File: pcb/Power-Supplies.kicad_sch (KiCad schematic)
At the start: 19 parts, among them U4 TLV62568DRL, U6 TLV75533PDRV, U7 TLV62568DRL

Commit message: Rev A Updates
Support LD2410S and LD2420 Radars in same connector as C4001. Now using 3.3V instead of 5V.
Removed Power control for Radars.
Added DS18S20 to measure CO sensor temperature directly.
Reworked SHT4X layout to reduce thermal transfer.
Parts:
- renumbered C14 to C10, C15 to C11, C16 to C12, C18 to C14, C19 to C15, C20 to C16, C21 to C17, C22 to C18, C23 to C19, C13 to C9, R3 to R1, R4 to R2, R6 to R4, R7 to R5, U4 to U2, U6 to U4, U7 to U5
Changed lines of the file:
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@@
 	(title_block
 		(title "ESPHome Parking Assistant")
-		(date "2025-04-18")
-		(rev "A")
+		(date "2025-09-23")
+		(rev "B")
 		(company "Mike Lawrence")
 	)
@@
 		(on_board yes)
 		(dnp no)
-		(property "Reference" "C16"
+		(property "Reference" "C12"
 			(at 152.4 128.524 0)
 			(effects
@@
 			(project "ESPHome-Indoor-Multi-Sensor"
 				(path "/e74956a0-c576-42e7-be96-7ce5c3135988/3a60bf96-310e-40eb-add5-f40abb45b52a"
-					(reference "C16")
+					(reference "C12")
 					(unit 1)
 				)
@@
 		(on_board yes)
 		(dnp no)
-		(property "Reference" "C14"
+		(property "Reference" "C10"
 			(at 129.54 128.524 0)
 			(effects
@@
 			(project "ESPHome-Indoor-Multi-Sensor"
 				(path "/e74956a0-c576-42e7-be96-7ce5c3135988/3a60bf96-310e-40eb-add5-f40abb45b52a"
-					(reference "C14")
+					(reference "C10")
 					(unit 1)
 				)
@@
 		(on_board yes)
 		(dnp no)
-		(property "Reference" "C20"
+		(property "Reference" "C16"
 			(at 95.25 65.024 0)
 			(effects
@@
 			(project "ESPHome-Indoor-Multi-Sensor"
 				(path "/e74956a0-c576-42e7-be96-7ce5c3135988/3a60bf96-310e-40eb-add5-f40abb45b52a"
-					(reference "C20")
+					(reference "C16")
 					(unit 1)
 				)
@@
 		(on_board yes)
 		(dnp no)
-		(property "Reference" "C21"
+		(property "Reference" "C17"
 			(at 154.94 65.024 0)
 			(effects
@@
 			(project "ESPHome-Indoor-Multi-Sensor"
 				(path "/e74956a0-c576-42e7-be96-7ce5c3135988/3a60bf96-310e-40eb-add5-f40abb45b52a"
-					(reference "C21")
+					(reference "C17")
 					(unit 1)
 				)
@@
 		(on_board yes)
 		(dnp no)
-		(property "Reference" "R7"
+		(property "Reference" "R5"
 			(at 144.018 69.85 0)
 			(effects
@@
 			(project "ESPHome-Indoor-Multi-Sensor"
 				(path "/e74956a0-c576-42e7-be96-7ce5c3135988/3a60bf96-310e-40eb-add5-f40abb45b52a"
-					(reference "R7")
+					(reference "R5")
 					(unit 1)
 				)
@@
 		(on_board yes)
 		(dnp no)
-		(property "Reference" "C13"
+		(property "Reference" "C9"
 			(at 69.85 128.524 0)
 			(effects
@@
 			(project "ESPHome-Indoor-Multi-Sensor"
 				(path "/e74956a0-c576-42e7-be96-7ce5c3135988/3a60bf96-310e-40eb-add5-f40abb45b52a"
-					(reference "C13")
+					(reference "C9")
 					(unit 1)
 				)
@@
 		(on_board yes)
 		(dnp no)
-		(property "Reference" "C22"
+		(property "Reference" "C18"
 			(at 166.37 65.024 0)
 			(effects
@@
 			(project "ESPHome-Indoor-Multi-Sensor"
 				(path "/e74956a0-c576-42e7-be96-7ce5c3135988/3a60bf96-310e-40eb-add5-f40abb45b52a"
-					(reference "C22")
+					(reference "C18")
 					(unit 1)
 				)
@@
 		(on_board yes)
 		(dnp no)
-		(property "Reference" "U6"
+		(property "Reference" "U4"
 			(at 177.8 112.014 0)
 			(effects
@@
 			(project ""
 				(path "/e74956a0-c576-42e7-be96-7ce5c3135988/3a60bf96-310e-40eb-add5-f40abb45b52a"
-					(reference "U6")
+					(reference "U4")
 					(unit 1)
 				)
@@
 		(on_board yes)
 		(dnp no)
-		(property "Reference" "R3"
+		(property "Reference" "R1"
 			(at 118.618 123.19 0)
 			(effects
@@
 			(project "ESPHome-Indoor-Multi-Sensor"
 				(path "/e74956a0-c576-42e7-be96-7ce5c3135988/3a60bf96-310e-40eb-add5-f40abb45b52a"
-					(reference "R3")
+					(reference "R1")
 					(unit 1)
 				)
@@
 		(on_board yes)
 		(dnp no)
-		(property "Reference" "C19"
+		(property "Reference" "C15"
 			(at 203.2 128.524 0)
 			(effects
@@
 			(project "ESPHome-Indoor-Multi-Sensor"
 				(path "/e74956a0-c576-42e7-be96-7ce5c3135988/3a60bf96-310e-40eb-add5-f40abb45b52a"
-					(reference "C19")
+					(reference "C15")
 					(unit 1)
 				)
@@
 		(on_board yes)
 		(dnp no)
-		(property "Reference" "R6"
+		(property "Reference" "R4"
 			(at 144.018 59.69 0)
 			(effects
@@
 			(project "ESPHome-Indoor-Multi-Sensor"
 				(path "/e74956a0-c576-42e7-be96-7ce5c3135988/3a60bf96-310e-40eb-add5-f40abb45b52a"
-					(reference "R6")
+					(reference "R4")
 					(unit 1)
 				)
@@
 		(on_board yes)
 		(dnp no)
-		(property "Reference" "U7"
+		(property "Reference" "U5"
 			(at 114.3 48.006 0)
 			(effects
@@
 			(project "ESPHome-Indoor-Multi-Sensor"
 				(path "/e74956a0-c576-42e7-be96-7ce5c3135988/3a60bf96-310e-40eb-add5-f40abb45b52a"
-					(reference "U7")
+					(reference "U5")
 					(unit 1)
 				)
@@
 		(on_board yes)
 		(dnp no)
-		(property "Reference" "C15"
+		(property "Reference" "C11"
 			(at 140.97 128.524 0)
 			(effects
@@
 			(project "ESPHome-Indoor-Multi-Sensor"
 				(path "/e74956a0-c576-42e7-be96-7ce5c3135988/3a60bf96-310e-40eb-add5-f40abb45b52a"
-					(reference "C15")
+					(reference "C11")
 					(unit 1)
 				)
@@
 		(on_board yes)
 		(dnp no)
-		(property "Reference" "C23"
+		(property "Reference" "C19"
 			(at 177.8 65.024 0)
 			(effects
@@
 			(project "ESPHome-Indoor-Multi-Sensor"
 				(path "/e74956a0-c576-42e7-be96-7ce5c3135988/3a60bf96-310e-40eb-add5-f40abb45b52a"
-					(reference "C23")
+					(reference "C19")
 					(unit 1)
 				)
@@
 		(on_board yes)
 		(dnp no)
-		(property "Reference" "U4"
+		(property "Reference" "U2"
 			(at 88.9 111.506 0)
 			(effects
@@
 			(project "ESPHome-Indoor-Multi-Sensor"
 				(path "/e74956a0-c576-42e7-be96-7ce5c3135988/3a60bf96-310e-40eb-add5-f40abb45b52a"
-					(reference "U4")
+					(reference "U2")
 					(unit 1)
 				)
@@
 		(on_board yes)
 		(dnp no)
-		(property "Reference" "R4"
+		(property "Reference" "R2"
 			(at 118.618 133.35 0)
 			(effects
@@
 			(project "ESPHome-Indoor-Multi-Sensor"
 				(path "/e74956a0-c576-42e7-be96-7ce5c3135988/3a60bf96-310e-40eb-add5-f40abb45b52a"
-					(reference "R4")
+					(reference "R2")
 					(unit 1)
 				)
@@
 		(on_board yes)
 		(dnp no)
-		(property "Reference" "C18"
+		(property "Reference" "C14"
 			(at 191.77 128.524 0)
 			(effects
@@
 			(project "ESPHome-Indoor-Multi-Sensor"
 				(path "/e74956a0-c576-42e7-be96-7ce5c3135988/3a60bf96-310e-40eb-add5-f40abb45b52a"
-					(reference "C18")
+					(reference "C14")
 					(unit 1)
 				)

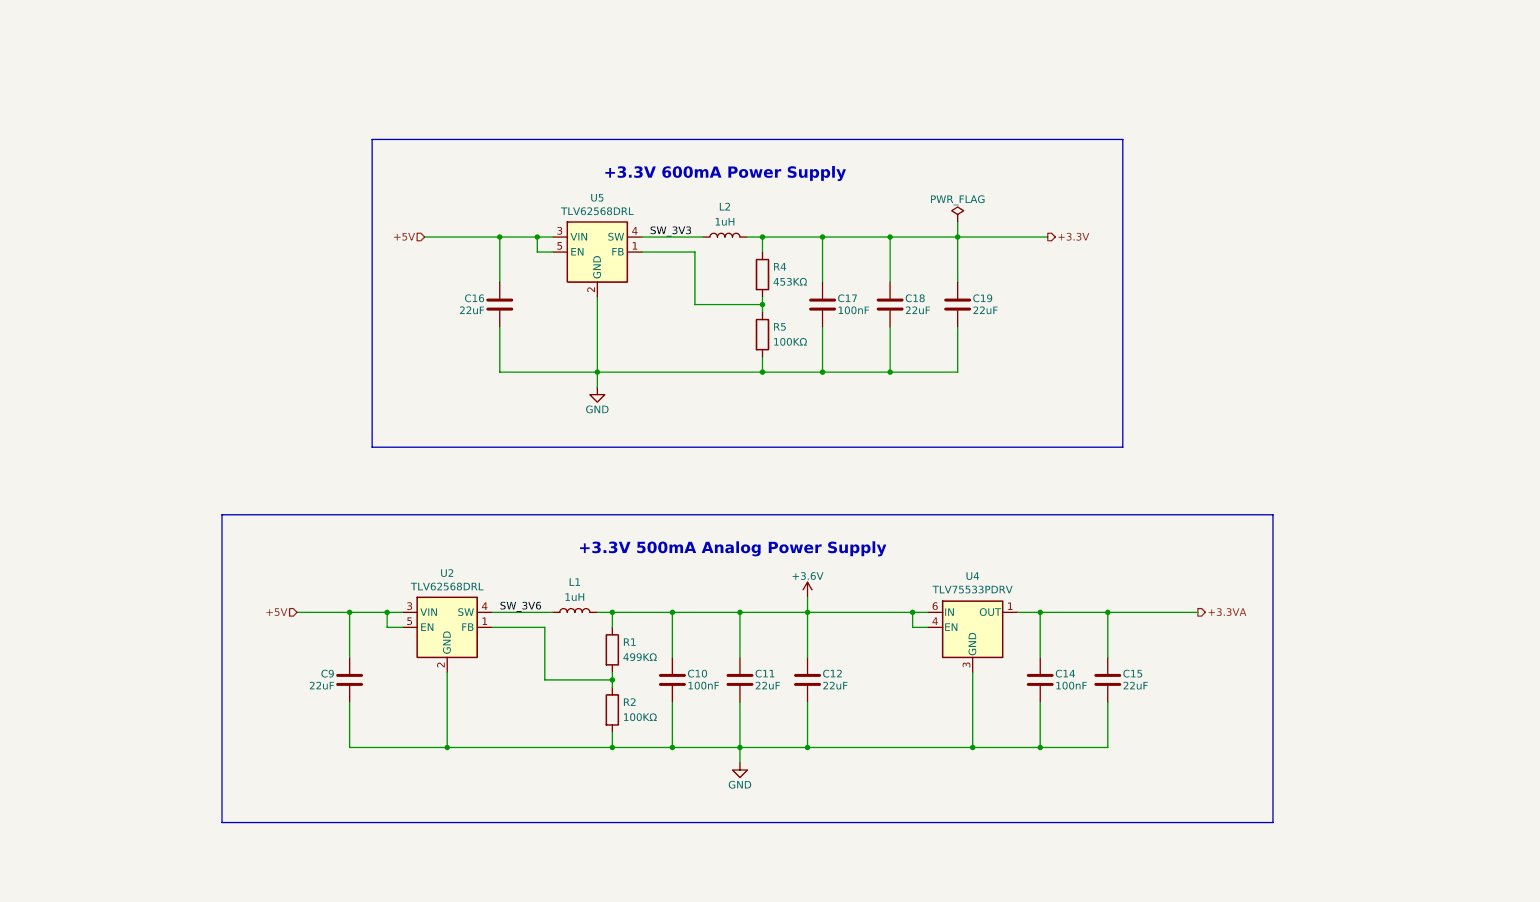
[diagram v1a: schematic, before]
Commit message: Add new ina228 to other power supplies
Not finished
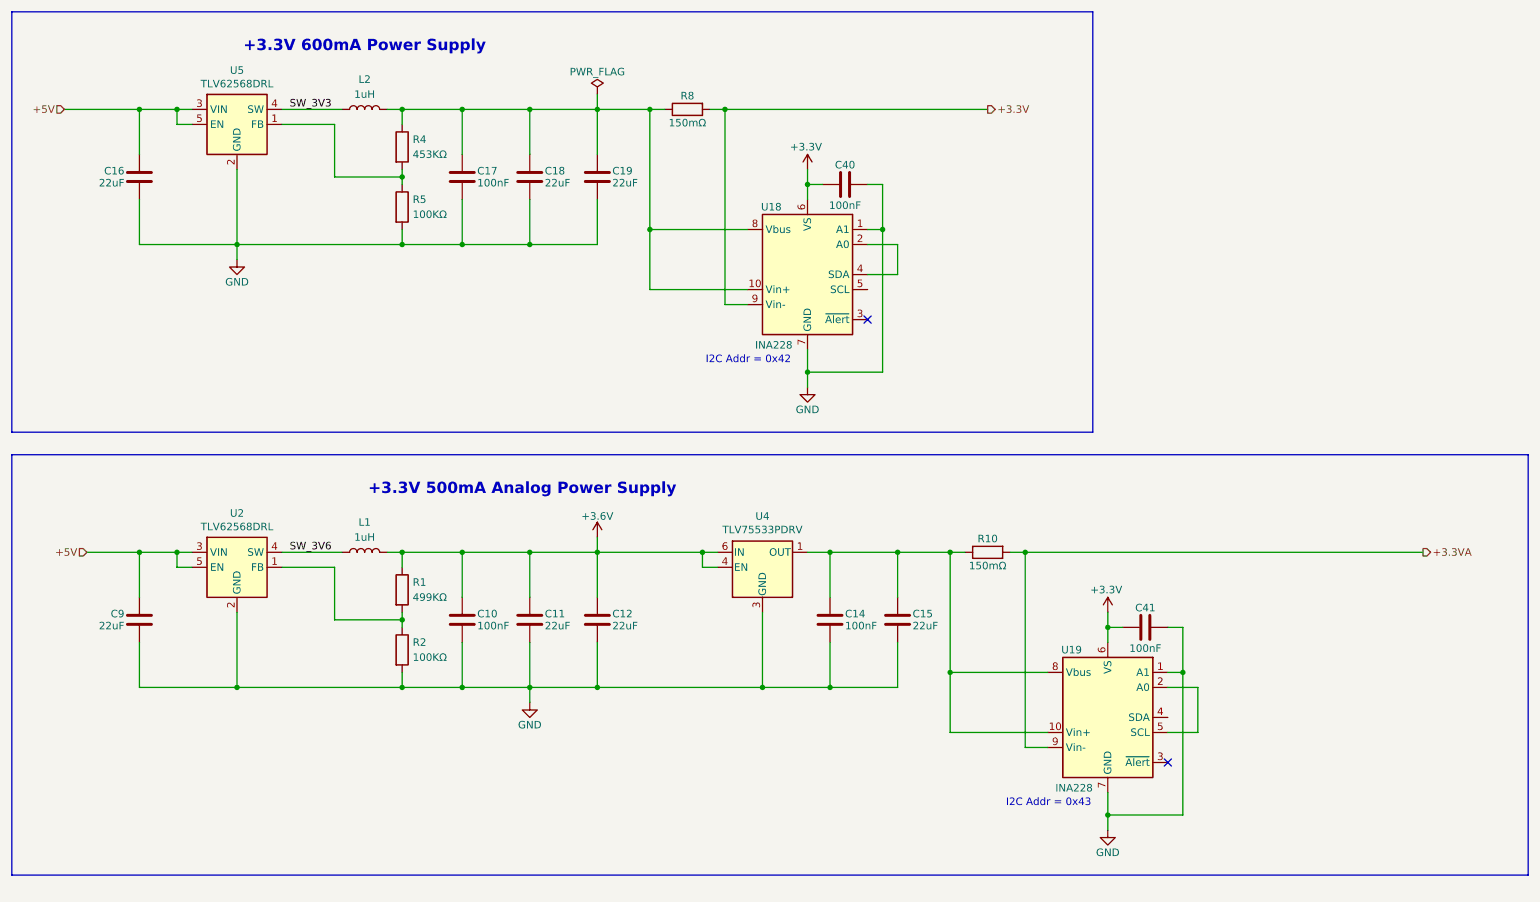
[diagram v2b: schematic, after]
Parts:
- added C40, C41: 100nF, Capacitor_SMD:C_0402_1005Metric, symbol Device:C
- added R10, R8: 150mΩ, Resistor_SMD:R_0603_1608Metric, symbol Device:R
- added U18, U19: INA228, Package_SO:VSSOP-10_3x3mm_P0.5mm, symbol Sensor_Energy:INA228
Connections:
- net +3.3V: now also C40.2, C41.2, R8.2, U18.6 (VS), U18.9 (Vin-), U19.6 (VS); no longer C17.2, C18.1, C19.1, L2.2, R4.1
- net +3.3VA: now also R10.2, U19.9 (Vin-); no longer C14.2, C15.1, U4.1 (OUT)
- net GND: now also C40.1, C41.1, U18.1 (A1), U18.7 (GND), U19.1 (A1), U19.7 (GND)
- new net: C17.2, C18.1, C19.1, L2.2, R4.1, R8.1, U18.10 (Vin+), U18.8 (Vbus)
- new net: C14.2, C15.1, R10.1, U19.10 (Vin+), U19.8 (Vbus), U4.1 (OUT)
- new net: U19.2 (A0), U19.5 (SCL)
- new net: U18.2 (A0), U18.4 (SDA)
- no-connect marks 0 -> 2
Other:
- note added: "I2C Addr = 0x42"
- note added: "I2C Addr = 0x43"
- moved on the sheet: C10, C11, C12, C14, C15, C16, C17, C18, C19, C9, L1, L2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

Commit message: Rev B Updates finish adding power monitors for 3.3V and 3.3VA
Removed speaker gain jumper
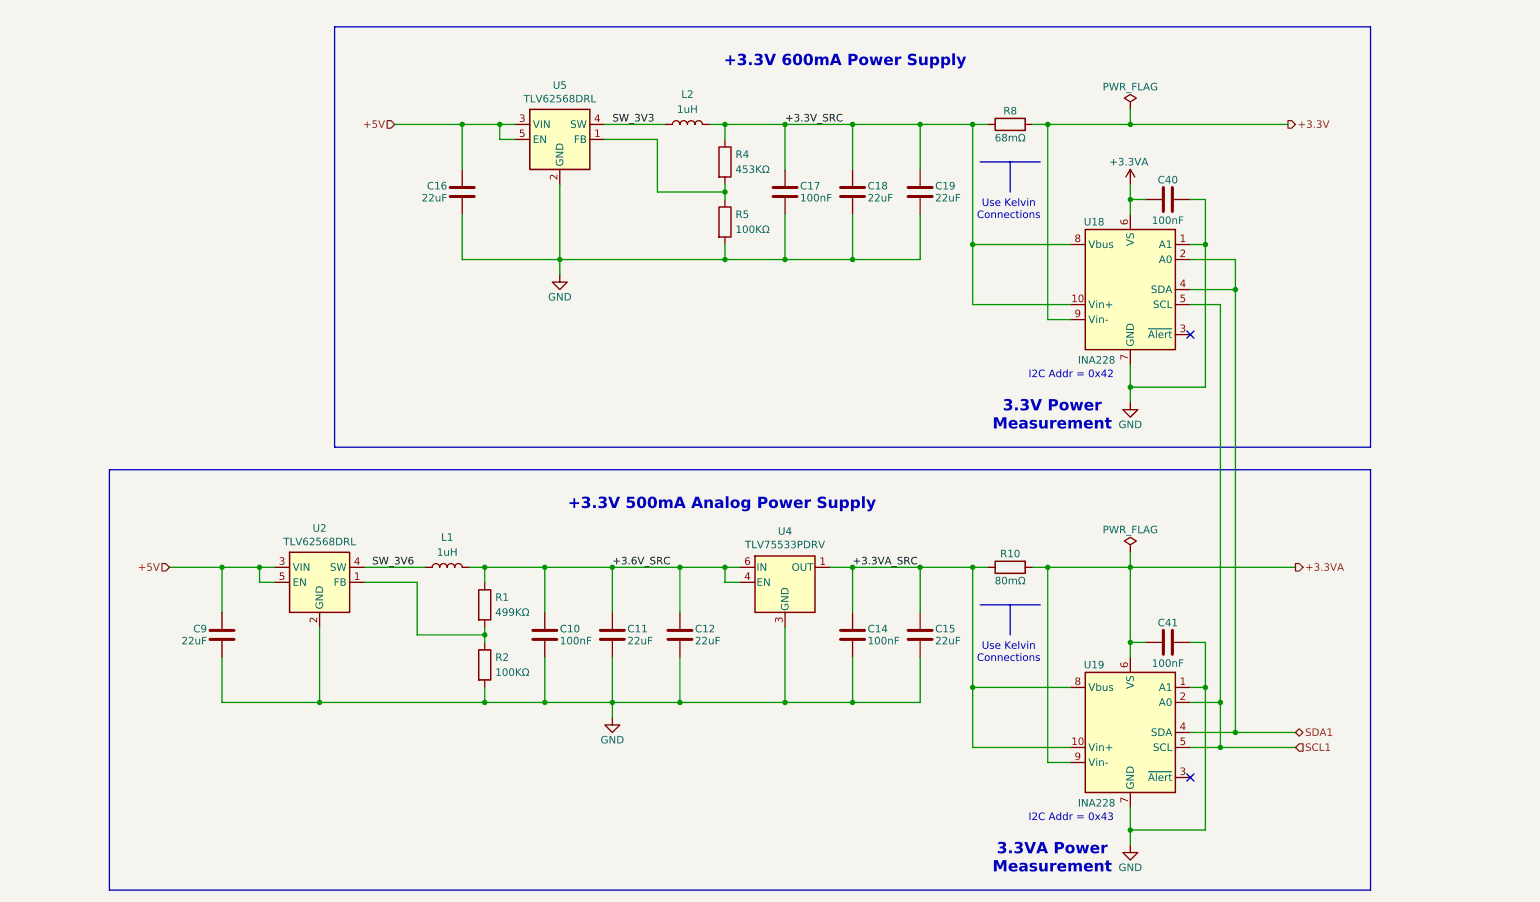
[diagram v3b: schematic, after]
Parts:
- R10: value 150mΩ -> 80mΩ; Manufacturer Panasonic -> Vishay; Part Number ERJ-14BSFR15U -> WSLP0603R0800FEB
- R8: value 150mΩ -> 68mΩ; Manufacturer Panasonic -> Vishay; Part Number ERJ-14BSFR15U -> WSLP0603R0680FEA
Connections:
- net +3.3V: no longer C40.2, C41.2, U18.6 (VS), U19.6 (VS)
- net +3.3VA: now also C40.2, C41.2, U18.6 (VS), U19.6 (VS)
- net +3.3V_SRC: now reaches C17.2, C18.1, C19.1, L2.2, R4.1, R8.1, U18.10 (Vin+), U18.8 (Vbus)
- net +3.3VA_SRC: now reaches C14.2, C15.1, R10.1, U19.10 (Vin+), U19.8 (Vbus), U4.1 (OUT)
- net SCL1: now reaches U19.2 (A0), U19.5 (SCL)
- net SCL1: now also U18.5 (SCL)
- net SDA1: now reaches U19.4 (SDA)
- net SDA1: now also U18.2 (A0), U18.4 (SDA)
- net +3.6V renamed +3.6V_SRC
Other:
- note added: "3.3V Power Measurement"
- note added: "3.3VA Power Measurement"
- note added: "Use Kelvin Connections"
- title: ESPHome Parking Assistant -> ESPHome Indoor Multi-Sensor
- moved on the sheet: C10, C11, C12, C14, C15, C16, C17, C18, C19, C40, C41, C9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

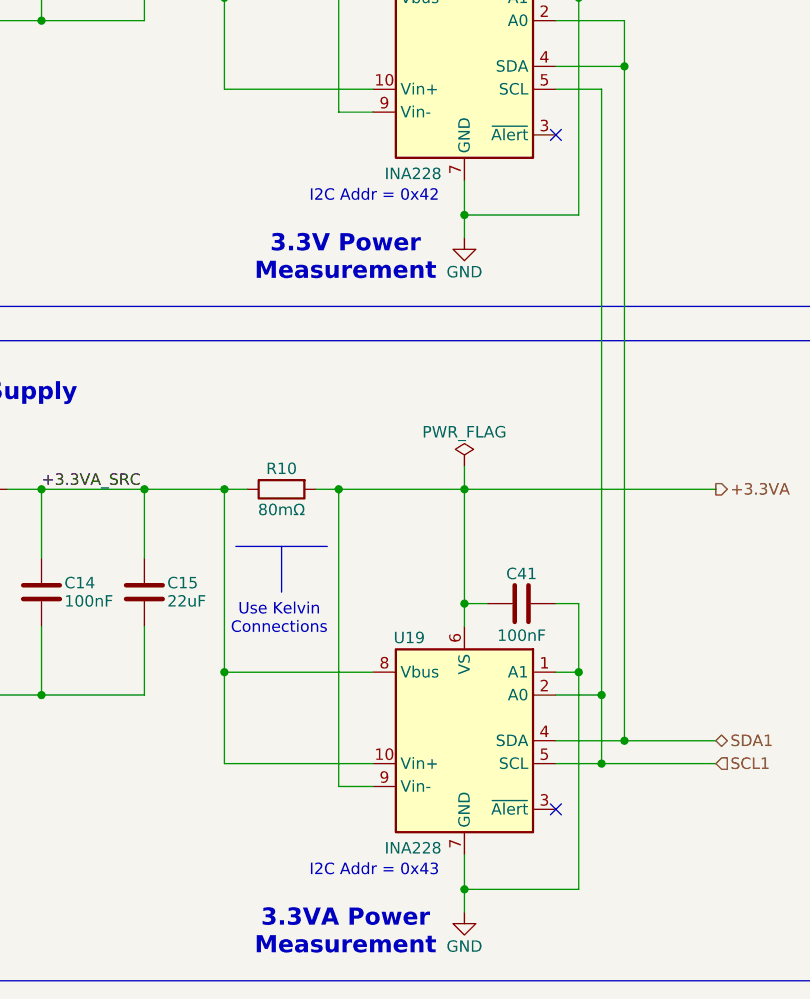
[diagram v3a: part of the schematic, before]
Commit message: BOM Updates
No PCB changes. This is still Rev.B
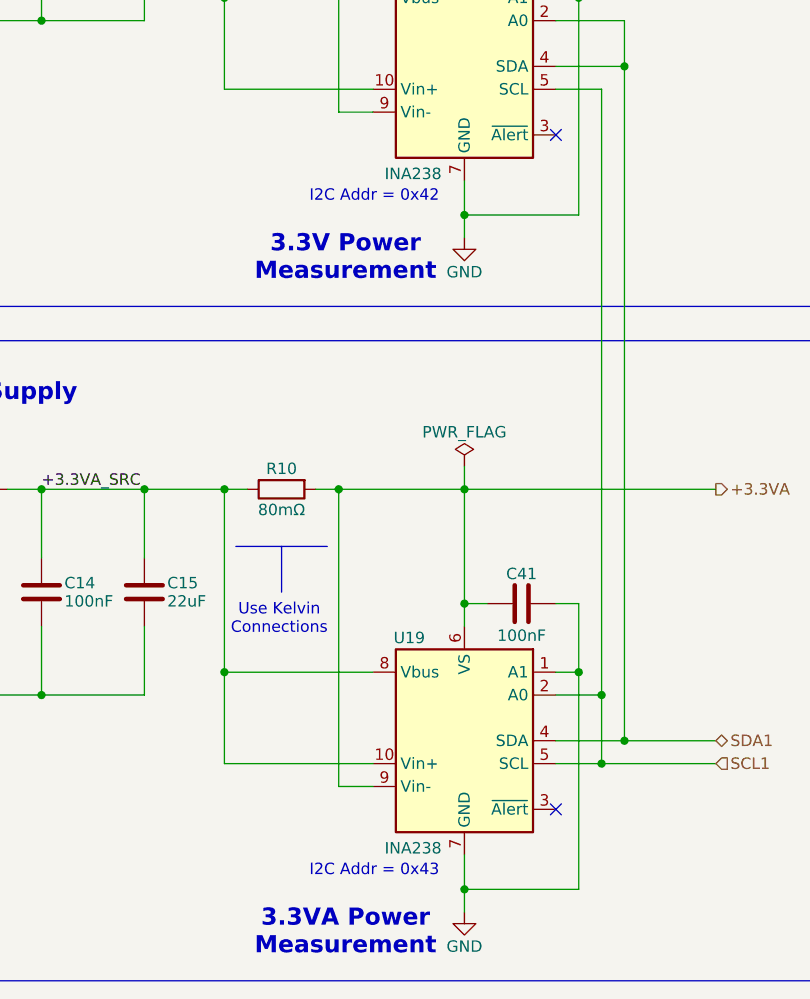
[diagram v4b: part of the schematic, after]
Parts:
- U18, U19: value INA228 -> INA238; Part Number INA228AIDGSR -> INA238AIDGSR
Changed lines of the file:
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@@
 			)
 		)
-		(property "Value" "INA228"
+		(property "Value" "INA238"
 			(at 201.93 150.368 0)
 			(effects
@@
 			)
 		)
-		(property "Description" "IC, High-Side or Low-Side Measurement, Bi-Directional Current and Power Monitor (0-85V) with I2C, SMBus-, and PMBus-Compatible Interface, VSSOP-10"
+		(property "Description" "IC, 85V, 16-Bit, High-Precision Power Monitor With I2C Interface, VSSOP-10"
 			(at 204.47 138.43 0)
 			(effects
@@
 			)
 		)
-		(property "Part Number" "INA228AIDGSR"
+		(property "Part Number" "INA238AIDGSR"
 			(at 204.47 138.43 0)
 			(effects
@@
 			)
 		)
-		(property "Value" "INA228"
+		(property "Value" "INA238"
 			(at 201.93 75.438 0)
 			(effects
@@
 			)
 		)
-		(property "Description" "IC, High-Side or Low-Side Measurement, Bi-Directional Current and Power Monitor (0-85V) with I2C, SMBus-, and PMBus-Compatible Interface, VSSOP-10"
+		(property "Description" "IC, 85V, 16-Bit, High-Precision Power Monitor With I2C Interface, VSSOP-10"
 			(at 204.47 63.5 0)
 			(effects
@@
 			)
 		)
-		(property "Part Number" "INA228AIDGSR"
+		(property "Part Number" "INA238AIDGSR"
 			(at 204.47 63.5 0)
 			(effects
